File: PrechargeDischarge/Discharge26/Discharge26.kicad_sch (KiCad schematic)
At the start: 7 parts, among them J1 HV_Conn, J2 LV_Conn, K4 Relay_SPST-NC, Q5 NMOS

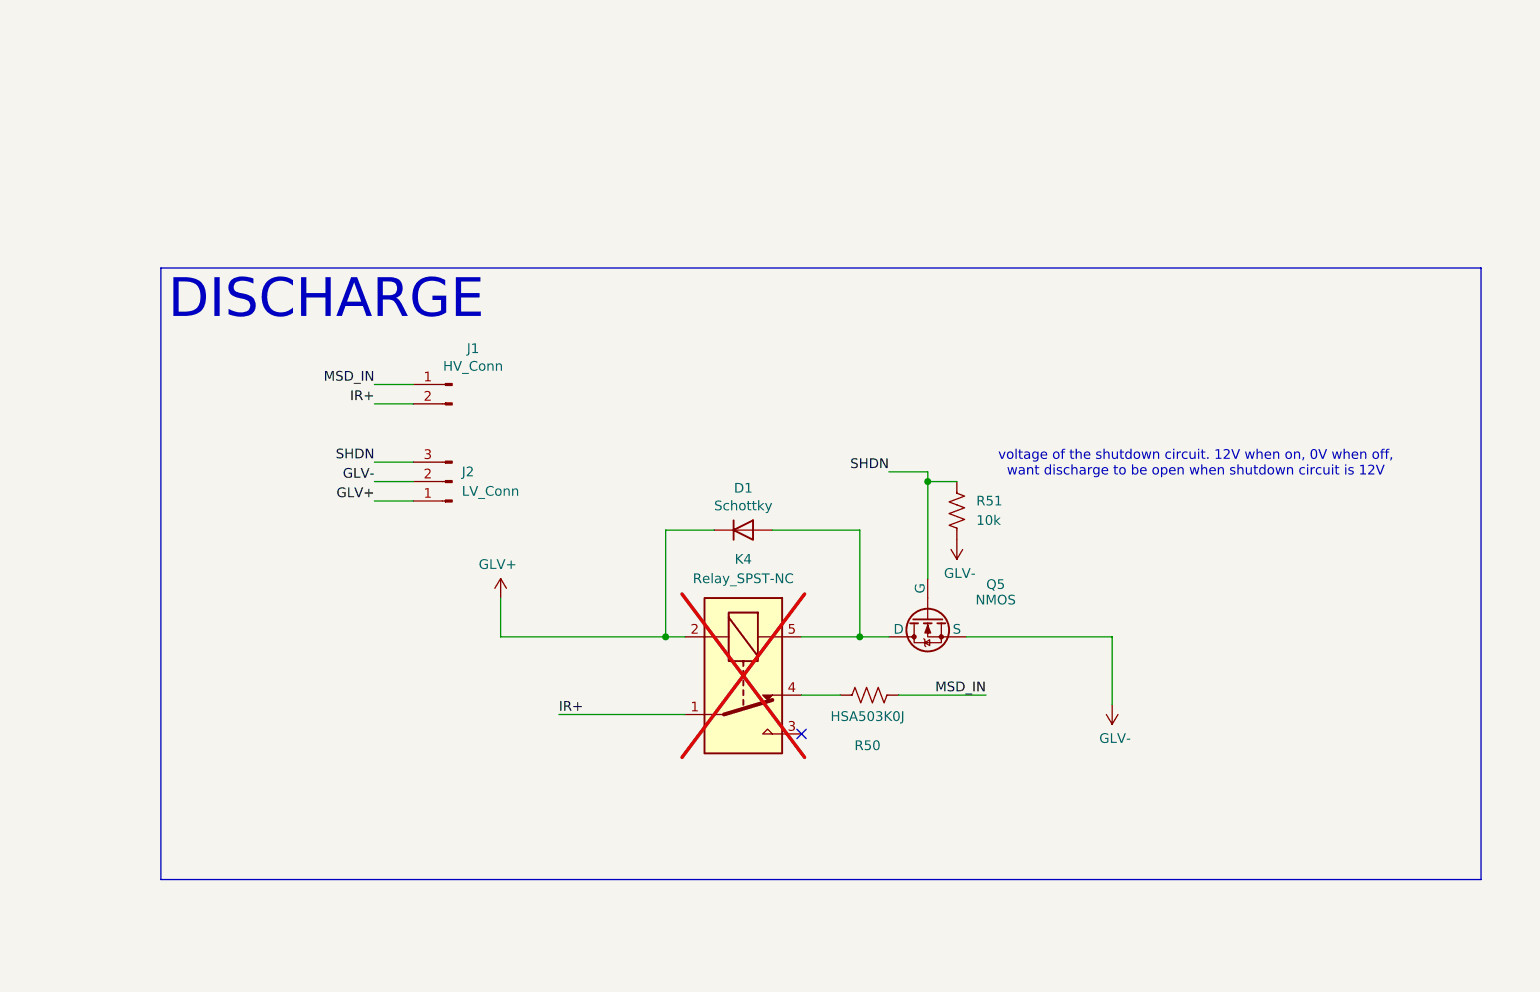
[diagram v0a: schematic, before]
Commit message: Precharge Testing
Uploaded precharge testing data, settled on 1.5k ohm resistor to precharge MC around 1s
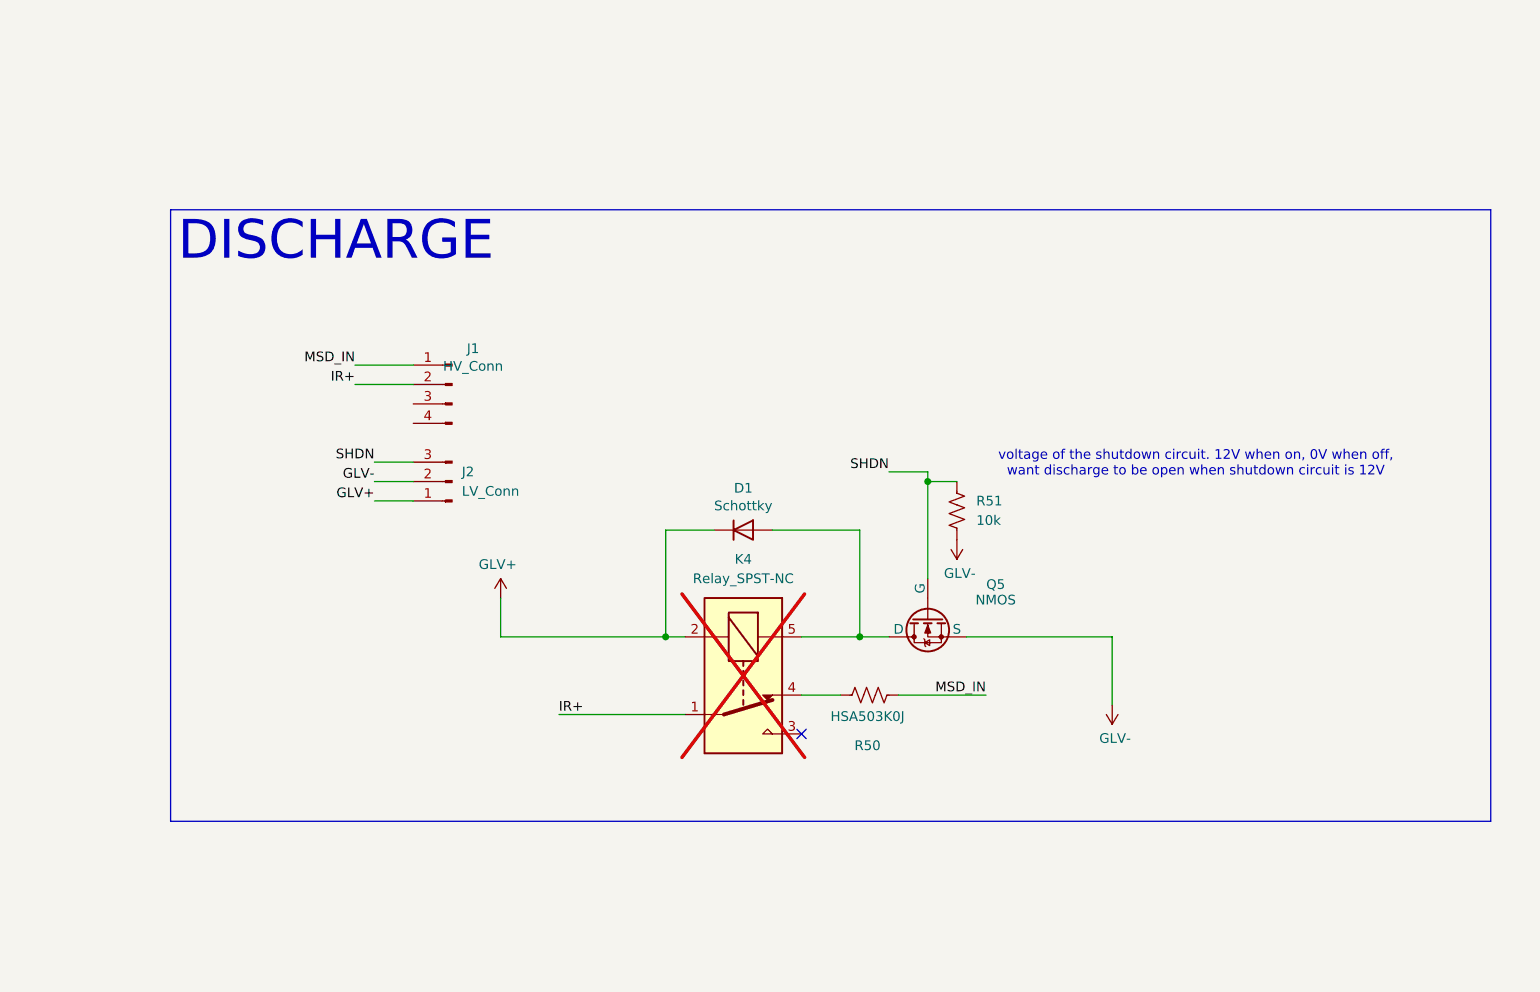
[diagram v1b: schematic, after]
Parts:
- J1: footprint Connector_Molex:Molex_Nano-Fit_105313-xx02_1x02_P2.50mm_Horizontal -> Discharge:MicroFit_4pin; symbol Connector:Conn_01x02_Pin -> Connector:Conn_01x04_Pin; JLC C564339 -> (none); MFR 1053131102 -> (none)
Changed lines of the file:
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@@
 	(text_box "DISCHARGE"
 		(exclude_from_sim no)
-		(at 45.72 53.34 0)
+		(at 46.99 45.72 0)
 		(size 172.72 80.01)
 		(margins 0.9525 0.9525 0.9525 0.9525)
@@
 	(wire
 		(pts
+			(xy 71.12 68.58) (xy 78.74 68.58)
+		)
+		(stroke
+			(width 0)
+			(type default)
+		)
+	)
+	(wire
+		(pts
 			(xy 90.17 101.6) (xy 111.76 101.6)
 		)
@@
 	(wire
 		(pts
-			(xy 73.66 68.58) (xy 78.74 68.58)
+			(xy 71.12 66.04) (xy 78.74 66.04)
 		)
 		(stroke
@@
 		(pts
 			(xy 137.16 101.6) (xy 140.97 101.6)
-		)
-		(stroke
-			(width 0)
-			(type default)
-		)
-	)
-	(wire
-		(pts
-			(xy 73.66 71.12) (xy 78.74 71.12)
 		)
 		(stroke
@@
 	)
 	(label "MSD_IN"
-		(at 73.66 68.58 180)
+		(at 71.12 66.04 180)
 		(effects
 			(font
@@
 	)
 	(label "IR+"
-		(at 73.66 71.12 180)
+		(at 71.12 68.58 180)
 		(effects
 			(font
@@
 	)
 	(symbol
-		(lib_id "Connector:Conn_01x02_Pin")
+		(lib_id "Connector:Conn_01x04_Pin")
 		(at 83.82 68.58 0)
 		(mirror y)
@@
 			)
 		)
-		(property "Footprint" "Connector_Molex:Molex_Nano-Fit_105313-xx02_1x02_P2.50mm_Horizontal"
+		(property "Footprint" "Discharge:MicroFit_4pin"
 			(at 83.82 68.58 0)
 			(effects
@@
 			)
 		)
-		(property "Datasheet" "https://www.molex.com/content/dam/molex/molex-dot-com/products/automated/en-us/salesdrawingpdf/105/105313/1053131102_sd.pdf?inline\\"
+		(property "Datasheet" "~"
 			(at 83.82 68.58 0)
 			(effects
@@
 			)
 		)
-		(property "Description" "Generic connector, single row, 01x02, script generated"
+		(property "Description" "Generic connector, single row, 01x04, script generated"
 			(at 83.82 68.58 0)
 			(effects
@@
 			)
 		)
-		(property "JLC" "C564339"
+		(property "JLC" ""
 			(at 83.82 68.58 0)
 			(effects
@@
 			)
 		)
-		(property "MFR" "1053131102"
+		(property "MFR" ""
 			(at 83.82 68.58 0)
 			(effects
@@
 		(pin "2"
 		)
+		(pin "3"
+		)
+		(pin "4"
+		)
 		(instances

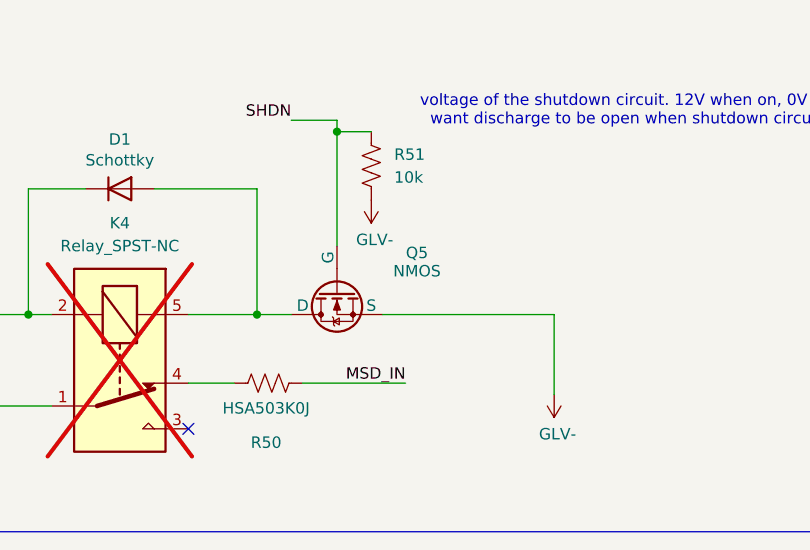
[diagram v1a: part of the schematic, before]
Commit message: Discharge fixes
Fixed footprint and symbol for discharge NMOS
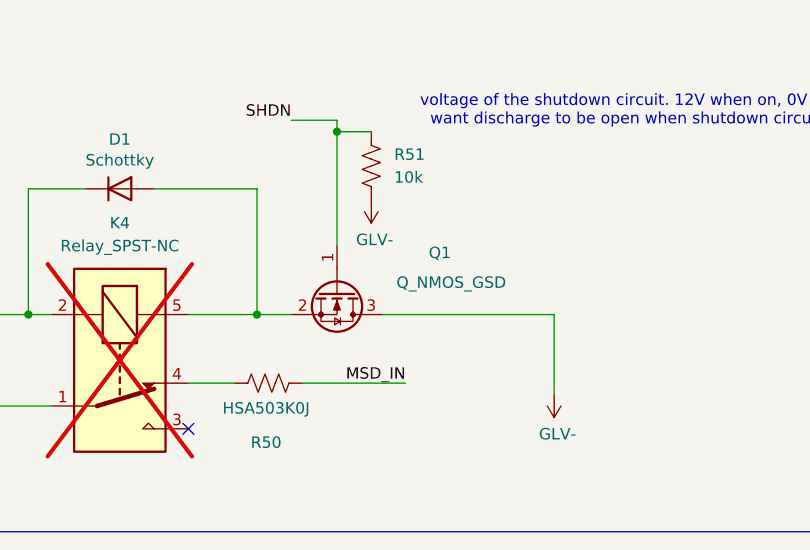
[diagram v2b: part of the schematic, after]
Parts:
- removed Q5: NMOS, Package_TO_SOT_SMD:SOT-23, symbol Simulation_SPICE:NMOS
- added Q1: Q_NMOS_GSD, Package_TO_SOT_SMD:SOT-23, symbol Transistor_FET:Q_NMOS_GSD
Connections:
- net GLV-: now also Q1.3 (D)
- net SHDN: now also Q1.1 (G)
- net at D1.2 (A), K4.5: now also Q1.2 (S)
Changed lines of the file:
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@@
+	)
+	(symbol
+		(lib_id "Transistor_FET:Q_NMOS_GSD")
+		(at 146.05 99.06 270)
+		(unit 1)
+		(exclude_from_sim no)
+		(in_bom yes)
+		(on_board yes)
+		(dnp no)
+		(property "Reference" "Q1"
+			(at 157.48 94.742 90)
+			(effects
+				(font
+					(size 1.27 1.27)
+				)
+			)
+		)
+		(property "Value" "Q_NMOS_GSD"
+			(at 158.75 98.044 90)
+			(effects
+				(font
+					(size 1.27 1.27)
+				)
+			)
+		)
+		(property "Footprint" "Package_TO_SOT_SMD:SOT-23"
+			(at 148.59 104.14 0)
+			(effects
+				(font
+					(size 1.27 1.27)
+				)
+				(hide yes)
+			)
+		)
+		(property "Datasheet" "https://jlcpcb.com/api/file/downloadByFileSystemAccessId/8550724090244980736"
+			(at 146.05 99.06 0)
+			(effects
+				(font
+					(size 1.27 1.27)
+				)
+				(hide yes)
+			)
+		)
+		(property "Description" "N-MOSFET transistor, gate/source/drain"
+			(at 146.05 99.06 0)
+			(effects
+				(font
+					(size 1.27 1.27)
+				)
+				(hide yes)
+			)
+		)
+		(property "JLC#" " C8545"
+			(at 146.05 99.06 90)
+			(effects
+				(font
+					(size 1.27 1.27)
+				)
+				(hide yes)
+			)
+		)
+		(pin "3"
+		)
+		(pin "2"
+		)
+		(pin "1"
+		)
+		(instances
+			(project ""
+				(path "/62b6171b-8267-4c49-8a4b-dd9e7963cbfb"
+					(reference "Q1")
+					(unit 1)
+				)
+			)
+		)
 	)
 	(symbol
@@
 					(unit 1)
 				)
-			)
-		)
-	)
-	(symbol
-		(lib_id "Simulation_SPICE:NMOS")
-		(at 146.05 99.06 90)
-		(mirror x)
-		(unit 1)
-		(exclude_from_sim no)
-		(in_bom yes)
-		(on_board yes)
-		(dnp no)
-		(property "Reference" "Q5"
-			(at 154.94 94.742 90)
-			(effects
-				(font
-					(size 1.27 1.27)
-				)
-			)
-		)
-		(property "Value" "NMOS"
-			(at 154.94 96.774 90)
-			(effects
-				(font
-					(size 1.27 1.27)
-				)
-			)
-		)
-		(property "Footprint" "Package_TO_SOT_SMD:SOT-23"
-			(at 143.51 104.14 0)
-			(effects
-				(font
-					(size 1.27 1.27)
-				)
-				(hide yes)
-			)
-		)
-		(property "Datasheet" ""
-			(at 158.75 99.06 0)
-			(effects
-				(font
-					(size 1.27 1.27)
-				)
-				(hide yes)
-			)
-		)
-		(property "Description" "N-MOSFET transistor, drain/source/gate"
-			(at 146.05 99.06 0)
-			(effects
-				(font
-					(size 1.27 1.27)
-				)
-				(hide yes)
-			)
-		)
-		(property "Sim.Device" "NMOS"
-			(at 163.195 99.06 0)
-			(effects
-				(font
-					(size 1.27 1.27)
-				)
-				(hide yes)
-			)
-		)
-		(property "Sim.Type" "VDMOS"
-			(at 165.1 99.06 0)
-			(effects
-				(font
-					(size 1.27 1.27)
-				)
-				(hide yes)
-			)
-		)
-		(property "Sim.Pins" "1=D 2=G 3=S"
-			(at 161.29 99.06 0)
-			(effects
-				(font
-					(size 1.27 1.27)
-				)
-				(hide yes)
-			)
-		)
-		(property "JLC" ""
-			(at 146.05 99.06 90)
-			(effects
-				(font
-					(size 1.27 1.27)
-				)
-				(hide yes)
-			)
-		)
-		(property "MFR" ""
-			(at 146.05 99.06 90)
-			(effects
-				(font
-					(size 1.27 1.27)
-				)
-				(hide yes)
-			)
-		)
-		(pin "1"
-		)
-		(pin "3"
-		)
-		(pin "2"
-		)
-		(instances
-			(project "Discharge26"
-				(path "/62b6171b-8267-4c49-8a4b-dd9e7963cbfb"
-					(reference "Q5")
-					(unit 1)
-				)

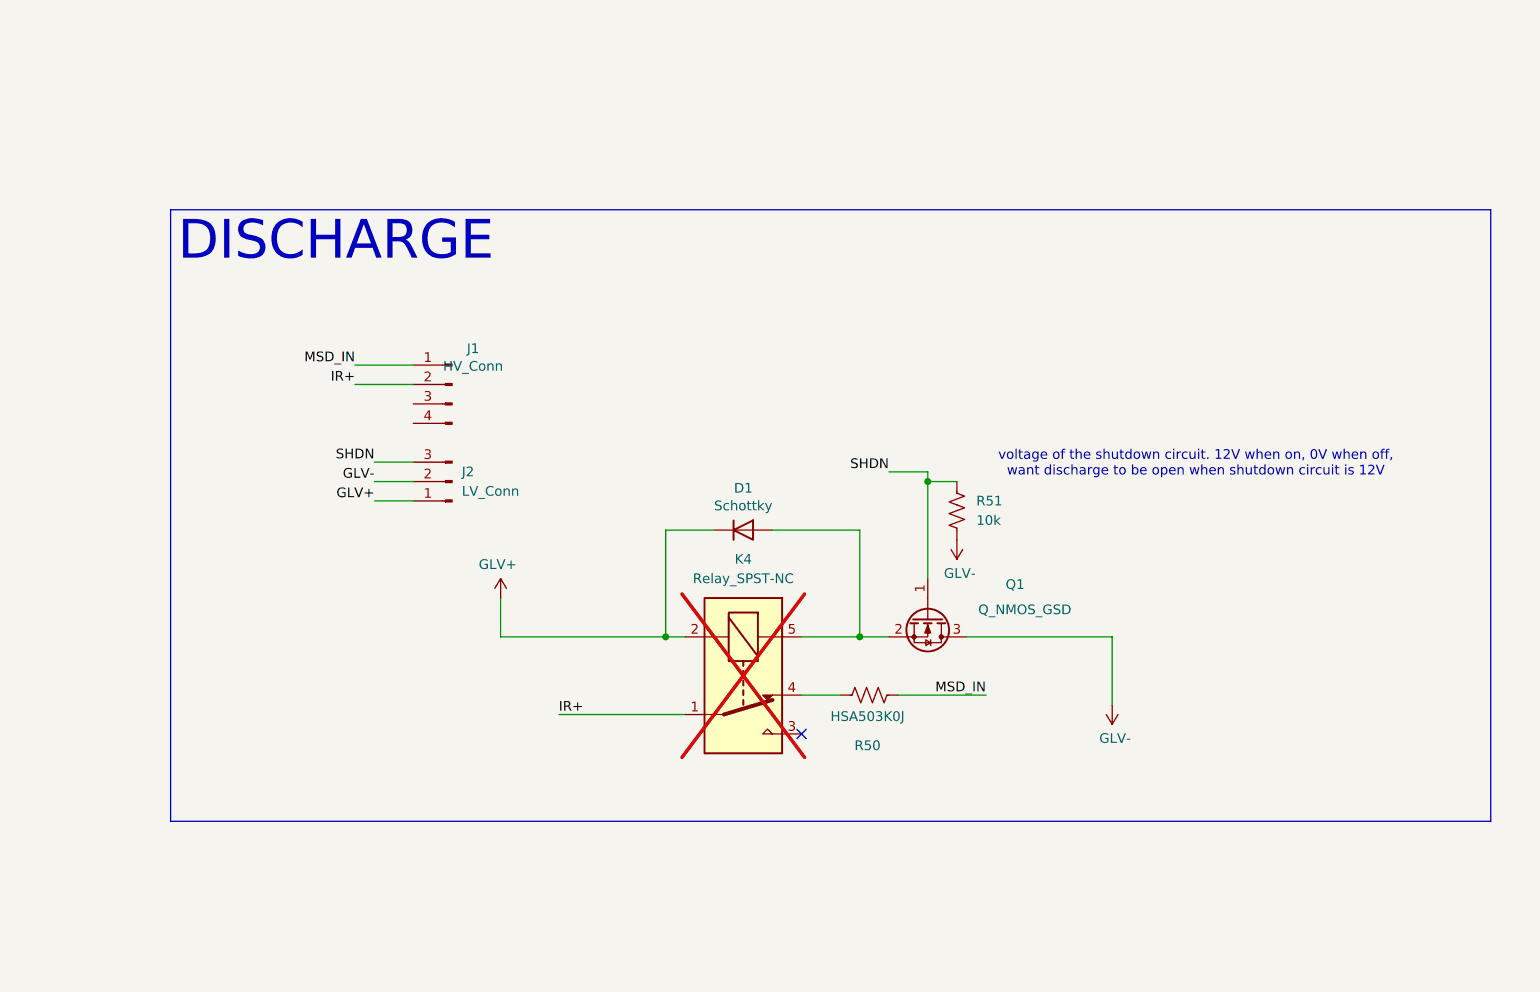
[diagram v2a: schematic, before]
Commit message: Fixed Discharge NMOS
Drain was connected to ground
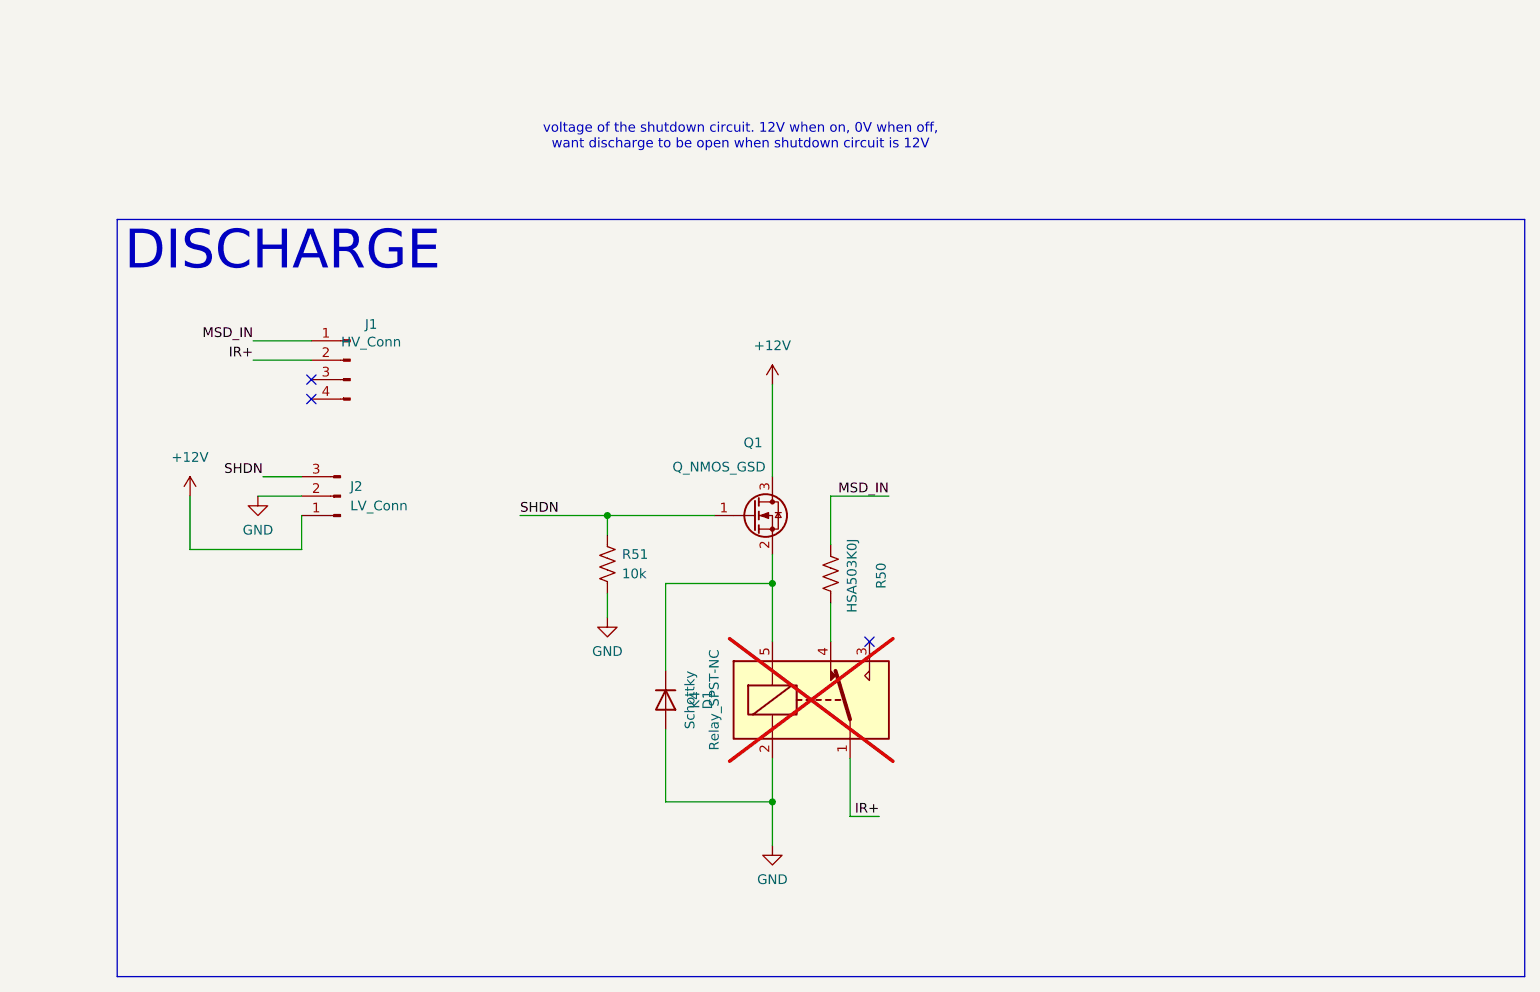
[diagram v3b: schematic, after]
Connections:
- net at K4.5, Q1.2 (S): now also D1.1 (K); no longer D1.2 (A)
- removed net GLV+: D1.1 (K), J2.1 (Pin_1), K4.2
- net GLV- renamed GND
- net GND: now also D1.2 (A), K4.2; no longer Q1.3 (D)
- new net +12V: J2.1 (Pin_1), Q1.3 (D)
- no-connect marks 1 -> 3
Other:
- moved on the sheet: D1, J1, J2, K4, Q1, R50, R51

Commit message: Discharge
guys its gonns work this time
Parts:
- added H1, H2, H3, H4: MountingHole, MountingHole:MountingHole_2.2mm_M2, symbol Mechanical:MountingHole
- K4: now fitted
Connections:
- net +12V: now also D1.1 (K), K4.2; no longer Q1.3 (D)
- net GND: now also Q1.2 (S); no longer D1.2 (A), K4.2
- new net: D1.2 (A), K4.5, Q1.3 (D)
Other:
- moved on the sheet: D1, J1, J2, Q1, R50, R51
